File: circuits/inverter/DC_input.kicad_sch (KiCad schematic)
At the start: 7 parts

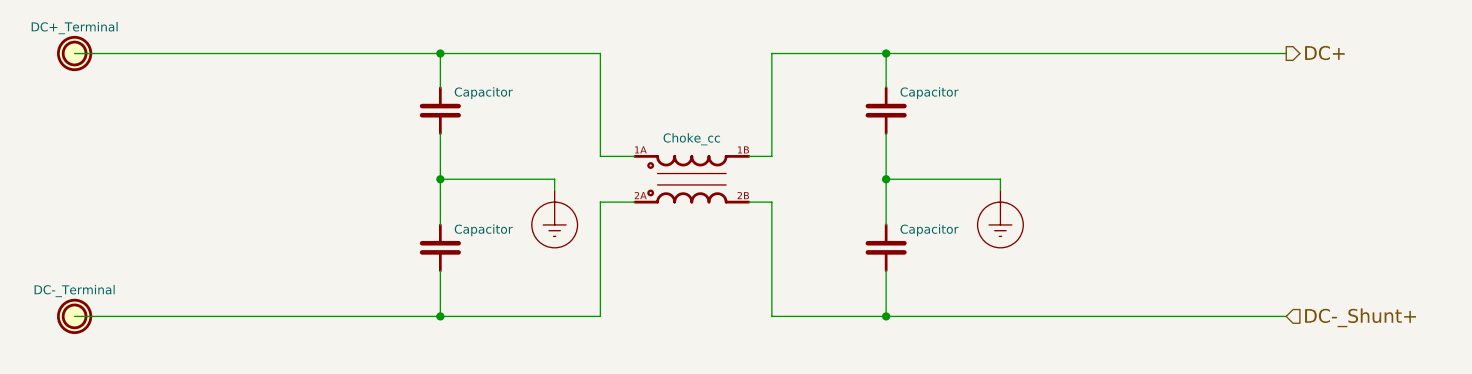
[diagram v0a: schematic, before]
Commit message: converts libraries to Kicad 6 format, updates bridge driver
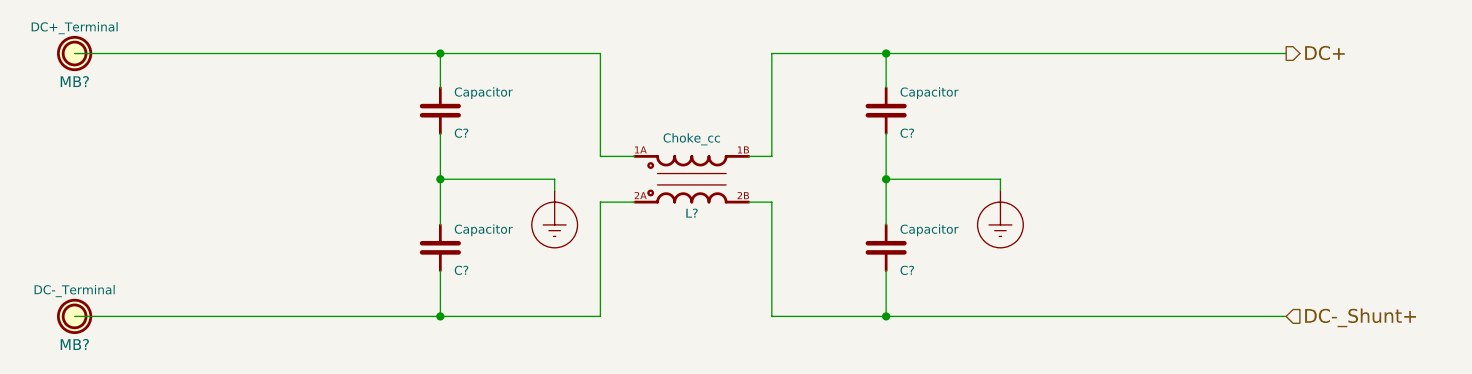
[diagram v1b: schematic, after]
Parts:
- gave numbers to parts that had none: 3
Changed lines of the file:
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@@
   (symbol (lib_id "OSSI_standard_components:Capacitor") (at 109.22 82.55 0) (unit 1)
     (in_bom yes) (on_board yes)
-    (property "Reference" "" (id 0) (at 110.744 85.09 0)
+    (property "Reference" "C?" (id 0) (at 110.744 85.09 0)
       (effects (font (size 0.9906 0.9906)) (justify left))
     )
@@
   (symbol (lib_id "OSSI_standard_components:Capacitor") (at 109.22 97.79 0) (unit 1)
     (in_bom yes) (on_board yes)
-    (property "Reference" "" (id 0) (at 110.744 100.33 0)
+    (property "Reference" "C?" (id 0) (at 110.744 100.33 0)
       (effects (font (size 0.9906 0.9906)) (justify left))
     )
@@
   (symbol (lib_id "OSSI_standard_components:Capacitor") (at 158.75 82.55 0) (unit 1)
     (in_bom yes) (on_board yes)
-    (property "Reference" "" (id 0) (at 160.274 85.09 0)
+    (property "Reference" "C?" (id 0) (at 160.274 85.09 0)
       (effects (font (size 0.9906 0.9906)) (justify left))
     )
@@
   (symbol (lib_id "OSSI_standard_components:Capacitor") (at 158.75 97.79 0) (unit 1)
     (in_bom yes) (on_board yes)
-    (property "Reference" "" (id 0) (at 160.274 100.33 0)
+    (property "Reference" "C?" (id 0) (at 160.274 100.33 0)
       (effects (font (size 0.9906 0.9906)) (justify left))
     )
@@
   (symbol (lib_id "OSSI_standard_components:Plated_hole") (at 68.58 76.2 0) (unit 1)
     (in_bom yes) (on_board yes)
-    (property "Reference" "" (id 0) (at 68.58 79.375 0)
+    (property "Reference" "MB?" (id 0) (at 68.58 79.375 0)
       (effects (font (size 1.1938 1.1938)))
     )
@@
   (symbol (lib_id "OSSI_standard_components:Plated_hole") (at 68.58 105.41 0) (unit 1)
     (in_bom yes) (on_board yes)
-    (property "Reference" "" (id 0) (at 68.58 108.585 0)
+    (property "Reference" "MB?" (id 0) (at 68.58 108.585 0)
       (effects (font (size 1.1938 1.1938)))
     )
@@
   (symbol (lib_id "OSSI_standard_components:Choke_cc") (at 137.16 90.17 0) (unit 1)
     (in_bom yes) (on_board yes)
-    (property "Reference" "" (id 0) (at 137.16 93.98 0)
+    (property "Reference" "L?" (id 0) (at 137.16 93.98 0)
       (effects (font (size 0.9906 0.9906)))
     )

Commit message: converts the project to Kicad 7
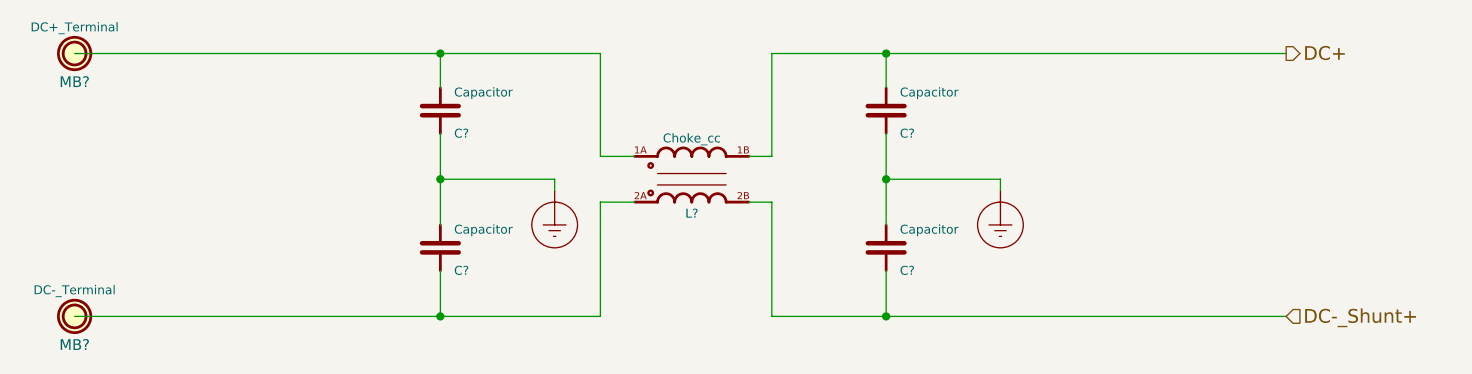
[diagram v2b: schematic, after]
